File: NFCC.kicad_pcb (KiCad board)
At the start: 4 copper layers, 90 x 70 mm, 105 parts, among them J1 USB_B_Micro, J2 USB_B_Micro, J3 LiPo Battery, SW5 SW_Push, SW6 SW_SPDT, U1 CH330N, U10 IIS2MDCTR, U11 24CW1280T-I/OT, U12 BMI088, U2 TPS54302, U3 LD39200PU33R, U7 BMP581, U8 W25N01GVZEIG, U9 PCA9685PW

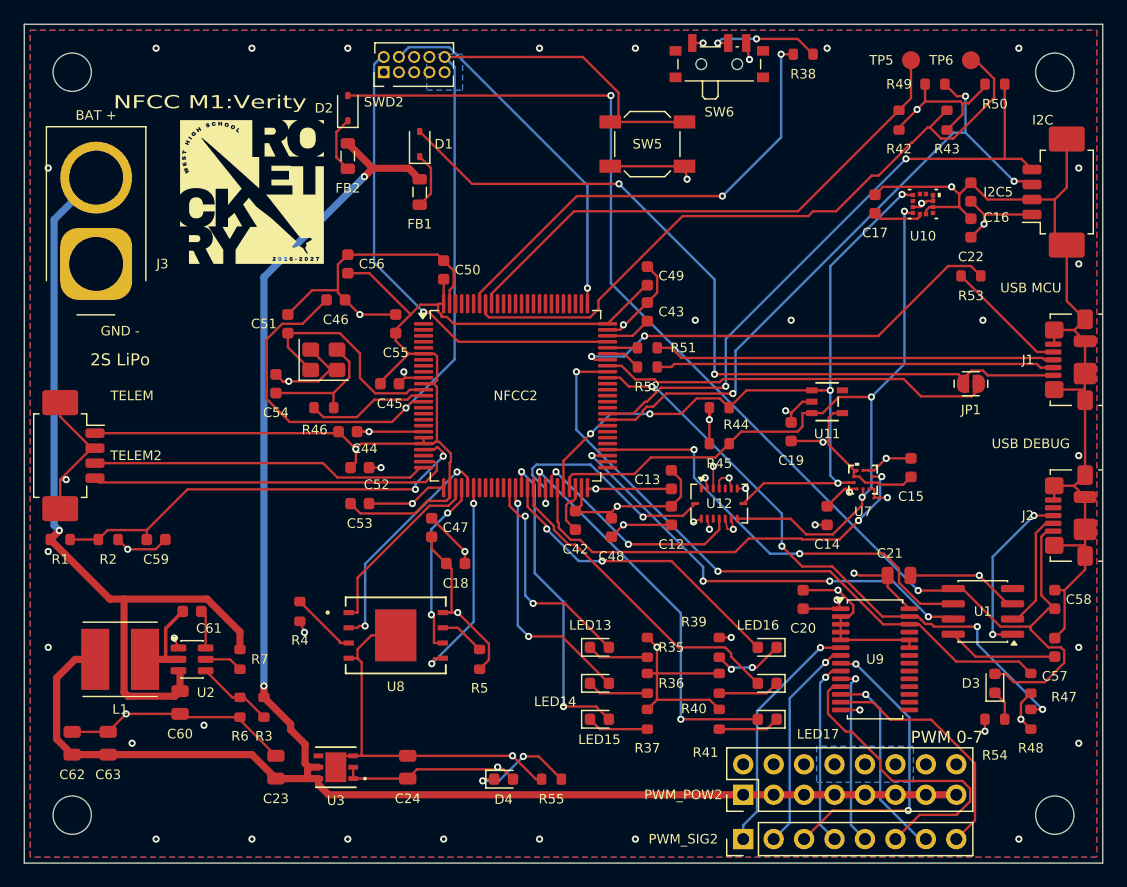
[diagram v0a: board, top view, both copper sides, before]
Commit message: Fix JLCPCB rule compliance and PWM header spacing
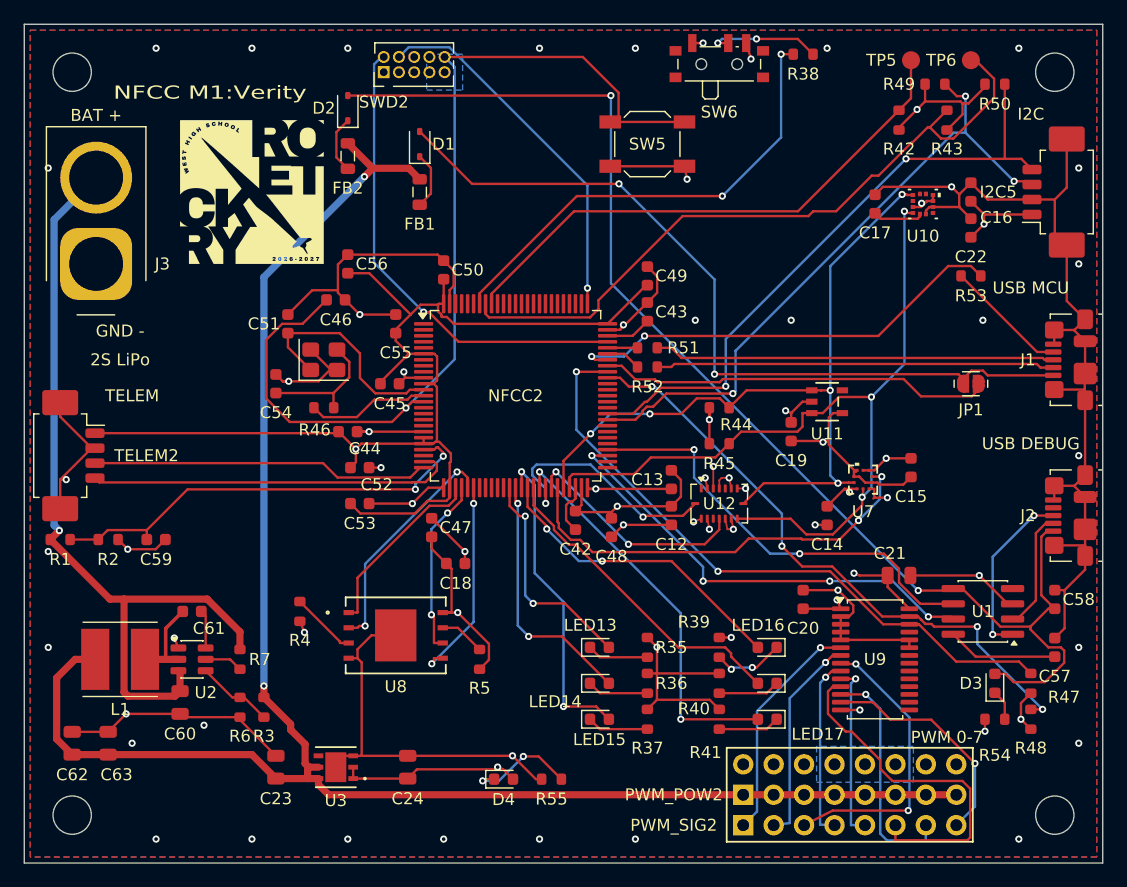
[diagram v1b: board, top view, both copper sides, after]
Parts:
- moved PWM_SIG2 1.16 mm to (120.0, 126.8)
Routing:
- net PWM_5: track 26.6 -> 29.6 mm
- net PWM_6: track 16.5 -> 19.5 mm
- net PWM_7: track 20.3 -> 19.1 mm, vias 0 -> 1
- net PWM_0: track 20.3 -> 19.2 mm
- net PWM_2: track 25.1 -> 24.4 mm
- net PWM_1: track 18.0 -> 17.5 mm

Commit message: Place I2C and telemetry connectors together on left edge
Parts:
- moved I2C5 88.0 mm to (63.5, 103.1), turned to -90 degrees
- moved R50 72.9 mm to (76.0, 98.0)
- moved R49 72.0 mm to (72.0, 98.0)
- moved C59 8.14 mm to (79.0, 104.5)
- moved R1 8.14 mm to (71.0, 104.5)
- moved R2 8.14 mm to (75.0, 104.5)
- moved TELEM2 5.10 mm to (63.5, 90.9)
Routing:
- net VDDA: track 207.1 -> 191.1 mm, vias 21 -> 23
- net BAT_SENSE: track 37.3 -> 28.8 mm
- net VBAT: track 67.1 -> 72.3 mm, vias 1 -> 2
- net I2C4_SDA: track 53.1 -> 49.1 mm
- net TELEM_RX: track 28.3 -> 30.6 mm, vias 0 -> 2
- net I2C4_SCL: track 54.4 -> 52.1 mm
- net TELEM_TX: track 30.8 -> 29.0 mm, vias 0 -> 2
- net GND: track 300.0 -> 299.3 mm, vias 56 -> 58
